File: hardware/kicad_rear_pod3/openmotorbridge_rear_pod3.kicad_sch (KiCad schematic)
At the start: 0 parts

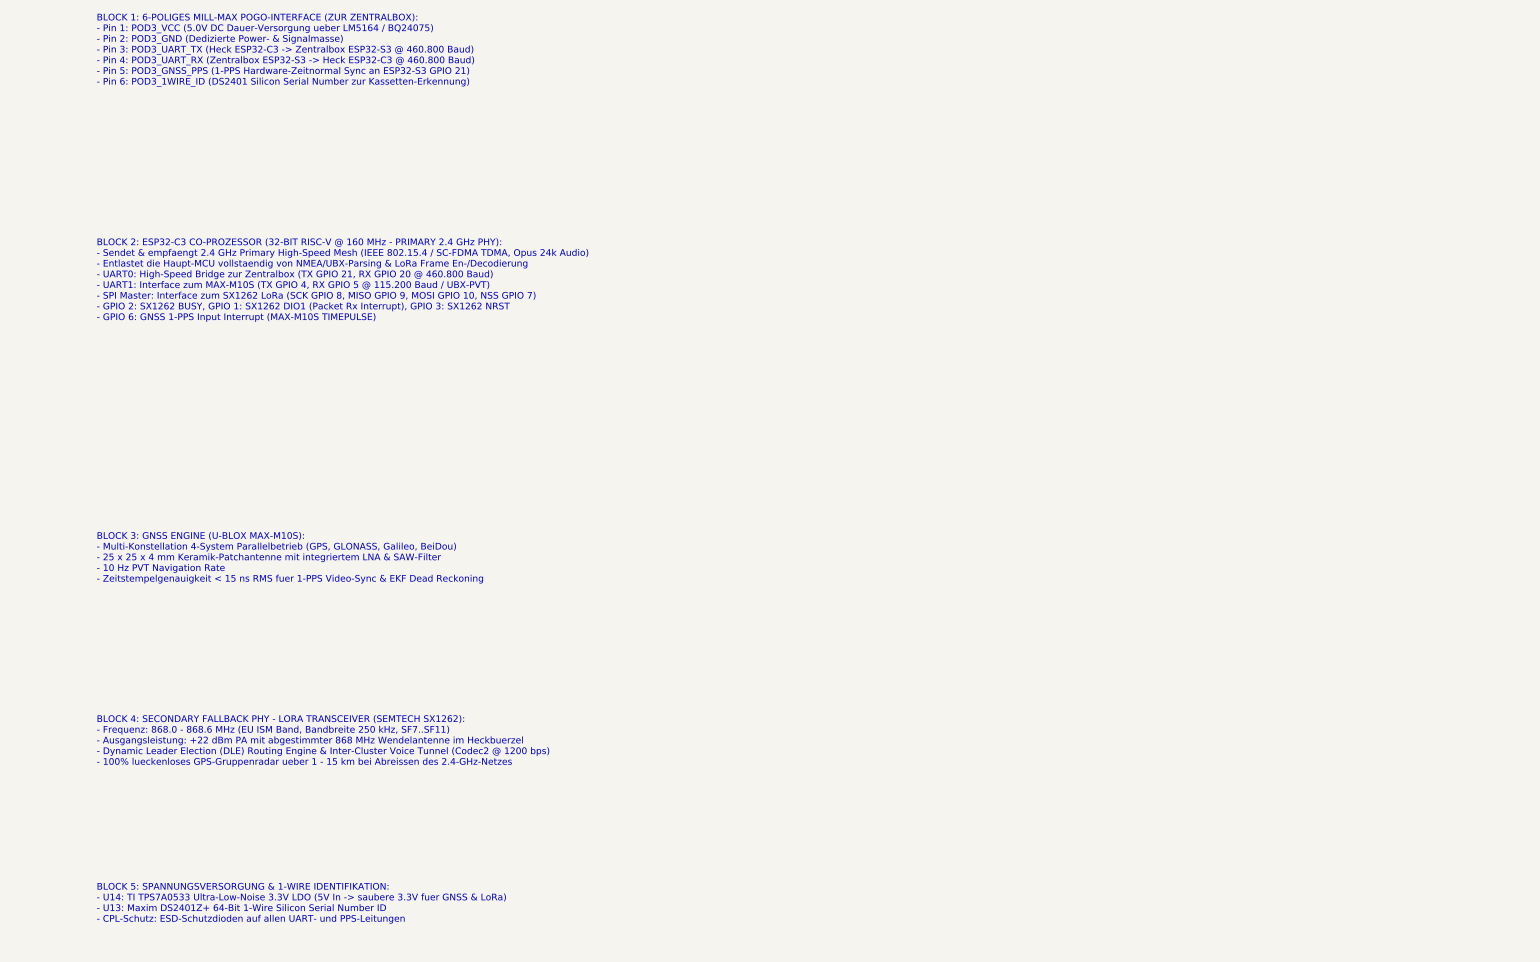
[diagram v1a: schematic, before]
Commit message: fix(kicad): Finalize KiCad 10 Pod 3 Transceiver and Universal Cartridge schematics and verified PDF exports
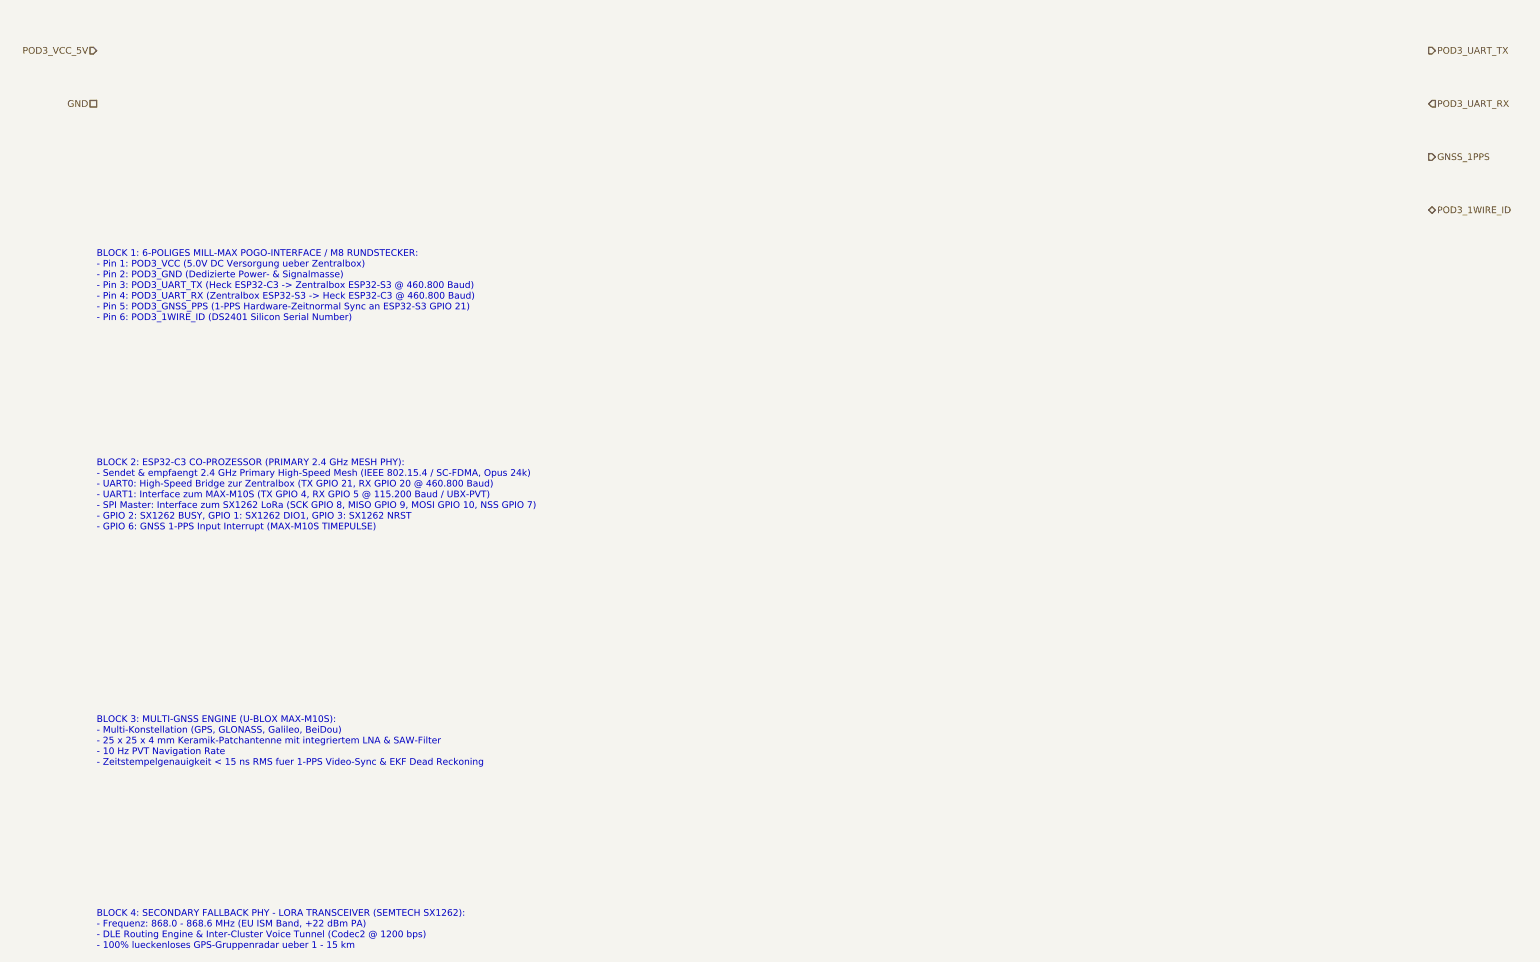
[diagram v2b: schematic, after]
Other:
- note added: "BLOCK 1: 6-POLIGES MILL-MAX POGO-INTERFACE / M8 RUNDSTECKER: - Pin 1: POD3_VCC (5.0V DC Versorgung ueber Zentralbox) - Pin 2: POD3_GND (Dedizierte Power- & Signalmasse) - Pin 3: POD3_UART_TX (Heck ESP32-C3 -> Zentralbox ESP32-S3 @ 460.800 Baud) - Pin 4: POD3_UART_RX (Zentralbox ESP32-S3 -> Heck ESP32-C3 @ 460.800 Baud) - Pin 5: POD3_GNSS_PPS (1-PPS Hardware-Zeitnormal Sync an ESP32-S3 GPIO 21) - 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"
- note added: "BLOCK 2: ESP32-C3 CO-PROZESSOR (PRIMARY 2.4 GHz MESH PHY): - Sendet & empfaengt 2.4 GHz Primary High-Speed Mesh (IEEE 802.15.4 / SC-FDMA, Opus 24k) - UART0: High-Speed Bridge zur Zentralbox (TX GPIO 21, RX GPIO 20 @ 460.800 Baud) - UART1: Interface zum MAX-M10S (TX GPIO 4, RX GPIO 5 @ 115.200 Baud / UBX-PVT) - SPI Master: Interface zum SX1262 LoRa (SCK GPIO 8, MISO GPIO 9, MOSI GPIO 10, NSS GPIO 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"
- note added: "BLOCK 3: MULTI-GNSS ENGINE (U-BLOX MAX-M10S): - Multi-Konstellation (GPS, GLONASS, Galileo, BeiDou) - 25 x 25 x 4 mm Keramik-Patchantenne mit integriertem LNA & SAW-Filter - 10 Hz PVT Navigation Rate - Zeitstempelgenauigkeit < 15 ns RMS fuer 1-PPS Video-Sync & EKF Dead Reckoning"
- note added: "BLOCK 4: SECONDARY FALLBACK PHY - LORA TRANSCEIVER (SEMTECH SX1262): - Frequenz: 868.0 - 868.6 MHz (EU ISM Band, +22 dBm PA) - DLE Routing Engine & Inter-Cluster Voice Tunnel (Codec2 @ 1200 bps) - 100% lueckenloses GPS-Gruppenradar ueber 1 - 15 km"
- note removed: "BLOCK 1: 6-POLIGES MILL-MAX POGO-INTERFACE (ZUR ZENTRALBOX): - Pin 1: POD3_VCC (5.0V DC Dauer-Versorgung ueber LM5164 / BQ24075) - Pin 2: POD3_GND (Dedizierte Power- & Signalmasse) - Pin 3: POD3_UART_TX (Heck ESP32-C3 -> Zentralbox ESP32-S3 @ 460.800 Baud) - Pin 4: POD3_UART_RX (Zentralbox ESP32-S3 -> Heck ESP32-C3 @ 460.800 Baud) - Pin 5: POD3_GNSS_PPS (1-PPS Hardware-Zeitnormal Sync an ESP32-S3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"
- note removed: "BLOCK 2: ESP32-C3 CO-PROZESSOR (32-BIT RISC-V @ 160 MHz - PRIMARY 2.4 GHz PHY): - Sendet & empfaengt 2.4 GHz Primary High-Speed Mesh (IEEE 802.15.4 / SC-FDMA TDMA, Opus 24k Audio) - Entlastet die Haupt-MCU vollstaendig von NMEA/UBX-Parsing & LoRa Frame En-/Decodierung - UART0: High-Speed Bridge zur Zentralbox (TX GPIO 21, RX GPIO 20 @ 460.800 Baud) - UART1: Interface zum MAX-M10S (TX GPIO 4, RX G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"
- note removed: "BLOCK 3: GNSS ENGINE (U-BLOX MAX-M10S): - Multi-Konstellation 4-System Parallelbetrieb (GPS, GLONASS, Galileo, BeiDou) - 25 x 25 x 4 mm Keramik-Patchantenne mit integriertem LNA & SAW-Filter - 10 Hz PVT Navigation Rate - Zeitstempelgenauigkeit < 15 ns RMS fuer 1-PPS Video-Sync & EKF Dead Reckoning"
- note removed: "BLOCK 4: SECONDARY FALLBACK PHY - LORA TRANSCEIVER (SEMTECH SX1262): - Frequenz: 868.0 - 868.6 MHz (EU ISM Band, Bandbreite 250 kHz, SF7..SF11) - Ausgangsleistung: +22 dBm PA mit abgestimmter 868 MHz Wendelantenne im Heckbuerzel - Dynamic Leader Election (DLE) Routing Engine & Inter-Cluster Voice Tunnel (Codec2 @ 1200 bps) - 100% lueckenloses GPS-Gruppenradar ueber 1 - 15 km bei Abreissen des 2.4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"
- note removed: "BLOCK 5: SPANNUNGSVERSORGUNG & 1-WIRE IDENTIFIKATION: - U14: TI TPS7A0533 Ultra-Low-Noise 3.3V LDO (5V In -> saubere 3.3V fuer GNSS & LoRa) - U13: Maxim DS2401Z+ 64-Bit 1-Wire Silicon Serial Number ID - CPL-Schutz: ESD-Schutzdioden auf allen UART- und PPS-Leitungen"
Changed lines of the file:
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@@
   (title_block
     (title "OpenMotorBridge v8.0 - Heck-Pod 3 (GNSS & Dual-PHY OpenMotorMesh)")
-    (date "2026-08-23")
+    (date "2026-08-24")
     (rev "v8.0")
     (company "OpenMotorBridge Open Source Hardware")
@@
     (comment 2 "Dual-PHY OMM Transceiver: 2.4 GHz HiFi Primary + 868 MHz Long-Range Fallback")
   )
-  (text "BLOCK 1: 6-POLIGES MILL-MAX POGO-INTERFACE (ZUR ZENTRALBOX):\n- Pin 1: POD3_VCC (5.0V DC Dauer-Versorgung ueber LM5164 / BQ24075)\n- Pin 2: POD3_GND (Dedizierte Power- & Signalmasse)\n- Pin 3: POD3_UART_TX (Heck ESP32-C3 -> Zentralbox ESP32-S3 @ 460.800 Baud)\n- Pin 4: POD3_UART_RX (Zentralbox ESP32-S3 -> Heck ESP32-C3 @ 460.800 Baud)\n- Pin 5: POD3_GNSS_PPS (1-PPS Hardware-Zeitnormal Sync an ESP32-S3 GPIO 21)\n- Pin 6: POD3_1WIRE_ID (DS2401 Silicon Serial Number zur Kassetten-Erkennung)" (at 25.4 45.0 0)
+  (hierarchical_label "POD3_VCC_5V" (shape input) (at 25.4 38.1 180)
+    (effects (font (size 1.27 1.27)) (justify right))
+  )
+  (hierarchical_label "GND" (shape passive) (at 25.4 48.26 180)
+    (effects (font (size 1.27 1.27)) (justify right))
+  )
+  (hierarchical_label "POD3_UART_TX" (shape output) (at 280.0 38.1 0)
+    (effects (font (size 1.27 1.27)) (justify left))
+  )
+  (hierarchical_label "POD3_UART_RX" (shape input) (at 280.0 48.26 0)
+    (effects (font (size 1.27 1.27)) (justify left))
+  )
+  (hierarchical_label "GNSS_1PPS" (shape output) (at 280.0 58.42 0)
+    (effects (font (size 1.27 1.27)) (justify left))
+  )
+  (hierarchical_label "POD3_1WIRE_ID" (shape bidirectional) (at 280.0 68.58 0)
+    (effects (font (size 1.27 1.27)) (justify left))
+  )
+  (text "BLOCK 1: 6-POLIGES MILL-MAX POGO-INTERFACE / M8 RUNDSTECKER:\n- Pin 1: POD3_VCC (5.0V DC Versorgung ueber Zentralbox)\n- Pin 2: POD3_GND (Dedizierte Power- & Signalmasse)\n- Pin 3: POD3_UART_TX (Heck ESP32-C3 -> Zentralbox ESP32-S3 @ 460.800 Baud)\n- Pin 4: POD3_UART_RX (Zentralbox ESP32-S3 -> Heck ESP32-C3 @ 460.800 Baud)\n- Pin 5: POD3_GNSS_PPS (1-PPS Hardware-Zeitnormal Sync an ESP32-S3 GPIO 21)\n- Pin 6: POD3_1WIRE_ID (DS2401 Silicon Serial Number)" (at 25.4 90.0 0)
     (effects (font (size 1.27 1.27)) (justify left bottom))
   )
-  (text "BLOCK 2: ESP32-C3 CO-PROZESSOR (32-BIT RISC-V @ 160 MHz - PRIMARY 2.4 GHz PHY):\n- Sendet & empfaengt 2.4 GHz Primary High-Speed Mesh (IEEE 802.15.4 / SC-FDMA TDMA, Opus 24k Audio)\n- Entlastet die Haupt-MCU vollstaendig von NMEA/UBX-Parsing & LoRa Frame En-/Decodierung\n- UART0: High-Speed Bridge zur Zentralbox (TX GPIO 21, RX GPIO 20 @ 460.800 Baud)\n- UART1: Interface zum MAX-M10S (TX GPIO 4, RX GPIO 5 @ 115.200 Baud / UBX-PVT)\n- SPI Master: Interface zum SX1262 LoRa (SCK GPIO 8, MISO GPIO 9, MOSI GPIO 10, NSS GPIO 7)\n- GPIO 2: SX1262 BUSY, GPIO 1: SX1262 DIO1 (Packet Rx Interrupt), GPIO 3: SX1262 NRST\n- GPIO 6: GNSS 1-PPS Input Interrupt (MAX-M10S TIMEPULSE)" (at 25.4 90.0 0)
+  (text "BLOCK 2: ESP32-C3 CO-PROZESSOR (PRIMARY 2.4 GHz MESH PHY):\n- Sendet & empfaengt 2.4 GHz Primary High-Speed Mesh (IEEE 802.15.4 / SC-FDMA, Opus 24k)\n- UART0: High-Speed Bridge zur Zentralbox (TX GPIO 21, RX GPIO 20 @ 460.800 Baud)\n- UART1: Interface zum MAX-M10S (TX GPIO 4, RX GPIO 5 @ 115.200 Baud / UBX-PVT)\n- SPI Master: Interface zum SX1262 LoRa (SCK GPIO 8, MISO GPIO 9, MOSI GPIO 10, NSS GPIO 7)\n- GPIO 2: SX1262 BUSY, GPIO 1: SX1262 DIO1, GPIO 3: SX1262 NRST\n- GPIO 6: GNSS 1-PPS Input Interrupt (MAX-M10S TIMEPULSE)" (at 25.4 130.0 0)
     (effects (font (size 1.27 1.27)) (justify left bottom))
   )
-  (text "BLOCK 3: GNSS ENGINE (U-BLOX MAX-M10S):\n- Multi-Konstellation 4-System Parallelbetrieb (GPS, GLONASS, Galileo, BeiDou)\n- 25 x 25 x 4 mm Keramik-Patchantenne mit integriertem LNA & SAW-Filter\n- 10 Hz PVT Navigation Rate\n- Zeitstempelgenauigkeit < 15 ns RMS fuer 1-PPS Video-Sync & EKF Dead Reckoning" (at 25.4 140.0 0)
+  (text "BLOCK 3: MULTI-GNSS ENGINE (U-BLOX MAX-M10S):\n- Multi-Konstellation (GPS, GLONASS, Galileo, BeiDou)\n- 25 x 25 x 4 mm Keramik-Patchantenne mit integriertem LNA & SAW-Filter\n- 10 Hz PVT Navigation Rate\n- Zeitstempelgenauigkeit < 15 ns RMS fuer 1-PPS Video-Sync & EKF Dead Reckoning" (at 25.4 175.0 0)
     (effects (font (size 1.27 1.27)) (justify left bottom))
   )
-  (text "BLOCK 4: SECONDARY FALLBACK PHY - LORA TRANSCEIVER (SEMTECH SX1262):\n- Frequenz: 868.0 - 868.6 MHz (EU ISM Band, Bandbreite 250 kHz, SF7..SF11)\n- Ausgangsleistung: +22 dBm PA mit abgestimmter 868 MHz Wendelantenne im Heckbuerzel\n- Dynamic Leader Election (DLE) Routing Engine & Inter-Cluster Voice Tunnel (Codec2 @ 1200 bps)\n- 100% lueckenloses GPS-Gruppenradar ueber 1 - 15 km bei Abreissen des 2.4-GHz-Netzes" (at 25.4 175.0 0)
+  (text "BLOCK 4: SECONDARY FALLBACK PHY - LORA TRANSCEIVER (SEMTECH SX1262):\n- Frequenz: 868.0 - 868.6 MHz (EU ISM Band, +22 dBm PA)\n- DLE Routing Engine & Inter-Cluster Voice Tunnel (Codec2 @ 1200 bps)\n- 100% lueckenloses GPS-Gruppenradar ueber 1 - 15 km" (at 25.4 210.0 0)
     (effects (font (size 1.27 1.27)) (justify left bottom))
   )
-  (text "BLOCK 5: SPANNUNGSVERSORGUNG & 1-WIRE IDENTIFIKATION:\n- U14: TI TPS7A0533 Ultra-Low-Noise 3.3V LDO (5V In -> saubere 3.3V fuer GNSS & LoRa)\n- U13: Maxim DS2401Z+ 64-Bit 1-Wire Silicon Serial Number ID\n- CPL-Schutz: ESD-Schutzdioden auf allen UART- und PPS-Leitungen" (at 25.4 205.0 0)
-    (effects (font (size 1.27 1.27)) (justify left bottom))
-  )
